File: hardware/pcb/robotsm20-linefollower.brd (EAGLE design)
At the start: 230 x 100 mm, 141 parts, among them Q5 BSS138LT3G, Q6 BSS138LT3G, Q7 BSS138LT3G, Q8 BSS138LT3G, U1 STM32F405RG

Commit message: Change resistor and pinheader to dipswitch for RXTXBT and BOOT12
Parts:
- removed BOOT_SELECT: (no value), CASE-Pinhead:2X03
- removed R19, R20: (no value), rcl:R0603
- added SW1: CTS_219-4LPST, CASE-Switches:DIPSWITCH_4P_SMD
- R17, R18: value (none) -> 10k
- moved R18 218.9 mm to (-91.4, -41.3)
- moved R17 218.8 mm to (-91.4, -36.2), turned to 0 degrees
- moved DEBUG_CONNECTOR 207.3 mm to (23.5, 3.17), turned to 180 degrees
- turned R21 to 0 degrees
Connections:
- net +3V3: now also SW1.A3, SW1.A4; no longer BOOT_SELECT.1, BOOT_SELECT.2
- net DGND: now also R17.1, R18.1; no longer BOOT_SELECT.5, BOOT_SELECT.6
- net N$26: now also R17.2, SW1.B4; no longer BOOT_SELECT.4
- net N$34: now also R18.2, SW1.B3; no longer BOOT_SELECT.3
- net RX: now also SW1.B1; no longer R17.2, R18.2
- net RX_BT: now also SW1.A1; no longer R17.1
- net RX_HEADER: no longer R18.1
- net TX: now also SW1.B2; no longer R19.2, R20.2
- net TX_BT: now also SW1.A2; no longer R19.1
- net TX_HEADER: no longer R20.1
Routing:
- net SWDIO: track 0.00 -> 202.4 mm, vias 0 -> 2
- net SWCLK: track 0.00 -> 202.3 mm, vias 0 -> 2
- net N$1: track 112.5 -> 158.7 mm, vias 0 -> 2
- net SDIO_CMD: track 0.00 -> 13.0 mm
- net SDIO_CK: track 0.00 -> 11.7 mm
- net RX_HEADER: track 16.7 -> 5.18 mm
- net DGND: track 205.4 -> 216.5 mm
- net SDIO_D0: track 0.00 -> 10.8 mm
- net RX: track 48.2 -> 43.0 mm
- net TX: track 49.5 -> 45.9 mm
- net +3V3: track 89.1 -> 86.5 mm
- net BTN_SEL: track 0.00 -> 1.91 mm
- net TX_HEADER: track 19.6 -> 18.1 mm

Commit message: Routed new dipswitch
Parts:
- moved SW1 215.5 mm to (87.0, 79.4), turned to 270 degrees
- moved R41 14.1 mm to (77.5, 86.4), turned to 195 degrees
- moved R42 13.7 mm to (85.7, 88.3), turned to 195 degrees
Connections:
- removed net RX_HEADER: UART_CONNECTOR.1
- removed net TX_HEADER: UART_CONNECTOR.2
- net RX: now also UART_CONNECTOR.1
- net TX: now also UART_CONNECTOR.2
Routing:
- net TX: track 45.9 -> 71.4 mm
- net RX: track 43.0 -> 67.4 mm
- net TX_HEADER: track 18.1 -> 0.00 mm
- net +3V3: track 86.5 -> 71.0 mm
- net TX_BT: track 2.93 -> 8.21 mm, vias 0 -> 1
- net RX_HEADER: track 5.18 -> 0.00 mm
- net RX_BT: track 2.93 -> 7.82 mm

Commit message: Switched RL encoder pins
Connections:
- net ENC_L_A: now also U1.21; no longer U1.15
- net ENC_L_B: now also U1.55; no longer U1.14
- net ENC_R_A: now also U1.15; no longer U1.21
- net ENC_R_B: now also U1.14; no longer U1.55
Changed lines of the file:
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@@
 <contactref element="MOTORDRIVER" pad="41"/>
 <contactref element="U1" pad="59"/>
-<wire x1="141.181" y1="64.346" x2="141.181" y2="66.7137" width="0.254" layer="1"/>
-<wire x1="117.7130625" y1="63.0428" x2="139.8778" y2="63.0428" width="0.254" layer="1"/>
-<wire x1="139.8778" y1="63.0428" x2="141.181" y2="64.346" width="0.254" layer="1"/>
+<wire x1="141.181" y1="64.981" x2="141.181" y2="66.7137" width="0.254" layer="1"/>
+<wire x1="117.7130625" y1="63.0428" x2="139.2428" y2="63.0428" width="0.254" layer="1"/>
+<wire x1="139.2428" y1="63.0428" x2="141.181" y2="64.981" width="0.254" layer="1"/>
 <wire x1="115.802" y1="60.3276" x2="115.802" y2="61.1317375" width="0.254" layer="1"/>
 <wire x1="115.802" y1="61.1317375" x2="117.7130625" y2="63.0428" width="0.254" layer="1"/>
@@
 <contactref element="MOTORDRIVER" pad="42"/>
 <contactref element="U1" pad="58"/>
-<wire x1="140.681" y1="66.7137" x2="140.681" y2="64.481" width="0.254" layer="1"/>
-<wire x1="139.6492" y1="63.4492" x2="117.544725" y2="63.4492" width="0.254" layer="1"/>
+<wire x1="140.681" y1="66.7137" x2="140.681" y2="65.116" width="0.254" layer="1"/>
+<wire x1="139.0142" y1="63.4492" x2="117.544725" y2="63.4492" width="0.254" layer="1"/>
 <wire x1="115.302" y1="61.206475" x2="115.302" y2="60.3276" width="0.254" layer="1"/>
-<wire x1="140.681" y1="64.481" x2="139.6492" y2="63.4492" width="0.254" layer="1"/>
+<wire x1="140.681" y1="65.116" x2="139.0142" y2="63.4492" width="0.254" layer="1"/>
 <wire x1="117.544725" y1="63.4492" x2="115.302" y2="61.206475" width="0.254" layer="1"/>
 </signal>
@@
 <wire x1="107.1" y1="67.31" x2="116.84" y2="85.51" width="0" layer="19" extent="1-1"/>
 <wire x1="86.546034375" y1="88.48499375" x2="91.395" y2="78.105" width="0" layer="19" extent="1-1"/>
-<wire x1="78.291034375" y1="86.57999375" x2="89.0524" y2="67.945" width="0" layer="19" extent="1-1"/>
-<wire x1="59.54220625" y1="77.1517125" x2="78.291034375" y2="86.57999375" width="0" layer="19" extent="1-1"/>
+<wire x1="78.291034375" y1="86.57999375" x2="86.546034375" y2="88.48499375" width="0" layer="19" extent="1-1"/>
+<wire x1="67.89555625" y1="87.04444375" x2="78.291034375" y2="86.57999375" width="0" layer="19" extent="1-1"/>
+<wire x1="59.54220625" y1="77.1517125" x2="67.89555625" y2="87.04444375" width="0" layer="19" extent="1-1"/>
 <wire x1="57.624271875" y1="77.000825" x2="59.54220625" y2="77.1517125" width="0" layer="19" extent="1-1"/>
 <wire x1="51.557565625" y1="80.015775" x2="57.624271875" y2="77.000825" width="0" layer="19" extent="1-1"/>
-<wire x1="67.89555625" y1="87.04444375" x2="59.54220625" y2="77.1517125" width="0" layer="19" extent="1-1"/>
 <wire x1="76.48" y1="129.755" x2="86.546034375" y2="88.48499375" width="0" layer="19" extent="1-1"/>
 <wire x1="-88.265" y1="-22.225" x2="51.557565625" y2="80.015775" width="0" layer="19" extent="1-1"/>
@@
 </signal>
 <signal name="ENC_L_B">
-<contactref element="U1" pad="14"/>
 <contactref element="ENC_L" pad="5"/>
-<wire x1="66.675" y1="29.5" x2="145.6023" y2="75.135" width="0" layer="19" extent="1-1"/>
+<contactref element="U1" pad="55"/>
+<wire x1="66.675" y1="29.5" x2="139.181" y2="66.7137" width="0" layer="19" extent="1-1"/>
 </signal>
 <signal name="VOLTM_BOOST">
@@
 </signal>
 <signal name="ENC_L_A">
-<contactref element="U1" pad="15"/>
 <contactref element="ENC_L" pad="6"/>
-<wire x1="66.675" y1="28" x2="145.6023" y2="75.635" width="0" layer="19" extent="1-1"/>
+<contactref element="U1" pad="21"/>
+<wire x1="66.675" y1="28" x2="141.681" y2="78.0563" width="0" layer="19" extent="1-1"/>
 </signal>
 <signal name="VOLTM_BATT">
@@
 </signal>
 <signal name="ENC_R_A">
-<contactref element="U1" pad="21"/>
 <contactref element="ENC_R" pad="6"/>
-<wire x1="162.56" y1="35.5" x2="141.681" y2="78.0563" width="0" layer="19" extent="1-1"/>
+<contactref element="U1" pad="15"/>
+<wire x1="162.56" y1="35.5" x2="145.6023" y2="75.635" width="0" layer="19" extent="1-1"/>
 </signal>
 <signal name="MUX2">
@@
 </signal>
 <signal name="ENC_R_B">
-<contactref element="U1" pad="55"/>
 <contactref element="ENC_R" pad="5"/>
-<wire x1="162.56" y1="34" x2="139.181" y2="66.7137" width="0" layer="19" extent="1-1"/>
+<contactref element="U1" pad="14"/>
+<wire x1="162.56" y1="34" x2="145.6023" y2="75.135" width="0" layer="19" extent="1-1"/>
 </signal>
 <signal name="SDIO_CK">
@@
 <wire x1="75.1586" y1="80.4164" x2="76.835" y2="80.4164" width="0.254" layer="1"/>
 <wire x1="69.0098375" y1="86.5651625" x2="75.1586" y2="80.4164" width="0.254" layer="1"/>
-<wire x1="76.835" y1="80.4164" x2="138.181" y2="66.7137" width="0" layer="19" extent="1-1"/>
+<wire x1="138.181" y1="66.7137" x2="76.835" y2="80.4164" width="0" layer="19" extent="1-1"/>
 </signal>
 <signal name="BTN_SEL">
@@
 <contactref element="R17" pad="2"/>
 <contactref element="SW1" pad="B4"/>
-<wire x1="-90.59" y1="-36.195" x2="82.595" y2="75.565" width="0" layer="19" extent="1-1"/>
-<wire x1="-77.255" y1="2.54" x2="-90.59" y2="-36.195" width="0" layer="19" extent="1-1"/>
+<wire x1="-77.255" y1="2.54" x2="82.595" y2="75.565" width="0" layer="19" extent="1-1"/>
+<wire x1="-90.59" y1="-36.195" x2="-77.255" y2="2.54" width="0" layer="19" extent="1-1"/>
 </signal>
 <signal name="N$34">
@@
 <contactref element="R18" pad="2"/>
 <contactref element="SW1" pad="B3"/>
-<wire x1="-90.59" y1="-41.275" x2="82.595" y2="78.105" width="0" layer="19" extent="1-1"/>
-<wire x1="-78.955" y1="7.62" x2="-90.59" y2="-41.275" width="0" layer="19" extent="1-1"/>
+<wire x1="-78.955" y1="7.62" x2="82.595" y2="78.105" width="0" layer="19" extent="1-1"/>
+<wire x1="-90.59" y1="-41.275" x2="-78.955" y2="7.62" width="0" layer="19" extent="1-1"/>
 </signal>
 <signal name="MOTOR_R-">
@@
 <wire x1="74.93" y1="80.01" x2="76.835" y2="80.01" width="0.254" layer="1"/>
 <wire x1="69.215" y1="85.725" x2="74.93" y2="80.01" width="0.254" layer="1"/>
-<wire x1="76.835" y1="80.01" x2="138.681" y2="66.7137" width="0" layer="19" extent="1-1"/>
+<wire x1="138.681" y1="66.7137" x2="76.835" y2="80.01" width="0" layer="19" extent="1-1"/>
 </signal>
 <signal name="N$20">
@@
 <wire x1="143.181" y1="66.7137" x2="150.075" y2="69.215" width="0" layer="19" extent="1-1"/>
 <wire x1="143.51" y1="62.015" x2="143.181" y2="66.7137" width="0" layer="19" extent="1-1"/>
-<wire x1="143.181" y1="78.0563" x2="150.075" y2="69.215" width="0" layer="19" extent="1-1"/>
-<wire x1="142.875" y1="82.13" x2="143.181" y2="78.0563" width="0" layer="19" extent="1-1"/>
-<wire x1="137.795" y1="82.13" x2="142.875" y2="82.13" width="0" layer="19" extent="1-1"/>
-<wire x1="135.89" y1="82.13" x2="137.795" y2="82.13" width="0" layer="19" extent="1-1"/>
 <wire x1="129.325" y1="66.675" x2="143.181" y2="66.7137" width="0" layer="19" extent="1-1"/>
-<wire x1="129.325" y1="68.58" x2="129.325" y2="66.675" width="0" layer="19" extent="1-1"/>
-<wire x1="107.1" y1="71.12" x2="129.325" y2="68.58" width="0" layer="19" extent="1-1"/>
-<wire x1="97.86" y1="82.453" x2="107.1" y2="71.12" width="0" layer="19" extent="1-1"/>
-<wire x1="91.225" y1="72.39" x2="97.86" y2="82.453" width="0" layer="19" extent="1-1"/>
-<wire x1="89.0524" y1="70.245" x2="91.225" y2="72.39" width="0" layer="19" extent="1-1"/>
-<wire x1="84.455" y1="67.945" x2="89.0524" y2="70.245" width="0" layer="19" extent="1-1"/>
-<wire x1="84.78" y1="66.895" x2="84.455" y2="67.945" width="0" layer="19" extent="1-1"/>
-<wire x1="85.725" y1="63.285" x2="84.78" y2="66.895" width="0" layer="19" extent="1-1"/>
-<wire x1="83.82" y1="71.97" x2="84.455" y2="67.945" width="0" layer="19" extent="1-1"/>
-<wire x1="81.915" y1="72.705" x2="83.82" y2="71.97" width="0" layer="19" extent="1-1"/>
-<wire x1="92.925" y1="63.5" x2="85.725" y2="63.285" width="0" layer="19" extent="1-1"/>
-<wire x1="111.213" y1="92.253" x2="97.86" y2="82.453" width="0" layer="19" extent="1-1"/>
-<wire x1="68.58" y1="62.23" x2="84.78" y2="66.895" width="0" layer="19" extent="1-1"/>
-<wire x1="56.2476875" y1="76.008084375" x2="68.58" y2="62.23" width="0" layer="19" extent="1-1"/>
-<wire x1="52.36545625" y1="77.172496875" x2="56.2476875" y2="76.008084375" width="0" layer="19" extent="1-1"/>
-<wire x1="70.020590625" y1="88.33295" x2="56.2476875" y2="76.008084375" width="0" layer="19" extent="1-1"/>
-<wire x1="76.960184375" y1="92.06295" x2="70.020590625" y2="88.33295" width="0" layer="19" extent="1-1"/>
 <wire x1="75.78" y1="116.205" x2="76.960184375" y2="92.06295" width="0" layer="19" extent="1-1"/>
 <wire x1="75.88" y1="118.915" x2="75.78" y2="116.205" width="0" layer="19" extent="1-1"/>

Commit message: Routed more compoents
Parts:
- moved U$6 327.9 mm to (222.2, 61.0)
- moved U$4 326.3 mm to (221.6, 61.0), flipped to the bottom
- moved R44 264.3 mm to (162.6, 76.8)
- moved R43 263.4 mm to (162.6, 78.7), turned to 180 degrees
- moved R18 210.4 mm to (80.0, 80.6)
- moved R17 205.4 mm to (80.0, 76.8)
- moved C40 203.2 mm to (149.2, 62.9), turned to 270 degrees
- moved C13 194.1 mm to (108.5, 8.64), turned to 180 degrees
- moved R16 173.9 mm to (80.0, 74.9)
- moved R13 173.4 mm to (80.0, 78.7), turned to 180 degrees
- moved LED1 117.1 mm to (147.3, 36.8), turned to 180 degrees
- moved R38 112.7 mm to (149.9, 41.9), turned to 270 degrees
- moved R36 109.3 mm to (147.3, 41.9), turned to 270 degrees
- moved Q6 109.2 mm to (151.1, 45.7), turned to 180 degrees
- moved R40 106.0 mm to (144.8, 41.9), turned to 270 degrees
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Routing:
- net V+: track 231.0 -> 362.8 mm
- net ENC_L_A: track 0.00 -> 113.3 mm, vias 0 -> 9
- net ENC_L_B: track 0.00 -> 109.8 mm, vias 0 -> 7
- net PWM_FAN_L: track 0.00 -> 95.3 mm, vias 0 -> 4
- net SDIO_CMD: track 13.0 -> 101.1 mm, vias 0 -> 4
- net SDIO_CK: track 11.7 -> 95.2 mm, vias 0 -> 4
- net BUZZER: track 6.18 -> 85.1 mm, vias 0 -> 2
- net SDIO_D0: track 10.8 -> 81.6 mm, vias 0 -> 2
- net BOOT0: track 0.00 -> 70.6 mm, vias 0 -> 2
- net DGND: track 216.5 -> 285.3 mm, vias 0 -> 5
- net BOOT1: track 0.00 -> 63.3 mm, vias 0 -> 2
- net ENC_R_B: track 0.00 -> 54.8 mm, vias 0 -> 2
- net ENC_R_A: track 0.00 -> 53.7 mm, vias 0 -> 2
- net !RESET: track 83.5 -> 137.1 mm, vias 0 -> 3
- net PWM_FAN_R: track 0.00 -> 43.7 mm, vias 0 -> 2
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
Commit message: Changed testpoint to TH and rerouted due to change in design
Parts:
- TP_12V, TP_1V8, TP_3V3, TP_5V: value TEST-POINT3X5 -> TEST_POINTPAD_HOLE; device Isaks Bibliotek:PAD.03X.05 -> MISC:PAD_HOLE
- moved TP_3V3 54.6 mm to (-31.1, -9.53)
- moved TP_5V 54.6 mm to (-31.1, -5.71)
- moved TP_12V 48.9 mm to (-31.1, -11.4)
- moved TP_1V8 48.9 mm to (-31.1, -7.62)
- moved LED2 15.3 mm to (204.5, 5.71)
- moved BTN_RESET 2.35 mm to (217.5, 11.0), turned to 90 degrees
- moved BTN_SEL 1.54 mm to (12.3, 12.3), turned to 270 degrees
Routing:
- net SWCLK: track 202.3 -> 157.8 mm
- net SWDIO: track 203.7 -> 162.2 mm
- net DGND: track 285.3 -> 266.4 mm
- net N$38: track 25.9 -> 10.4 mm
- net N$1: track 158.7 -> 146.6 mm
- net !RESET: track 137.1 -> 126.8 mm
- net V+: track 362.8 -> 371.2 mm
- net N$41: track 42.5 -> 39.8 mm
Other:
- outline, holes or cut-outs redrawn

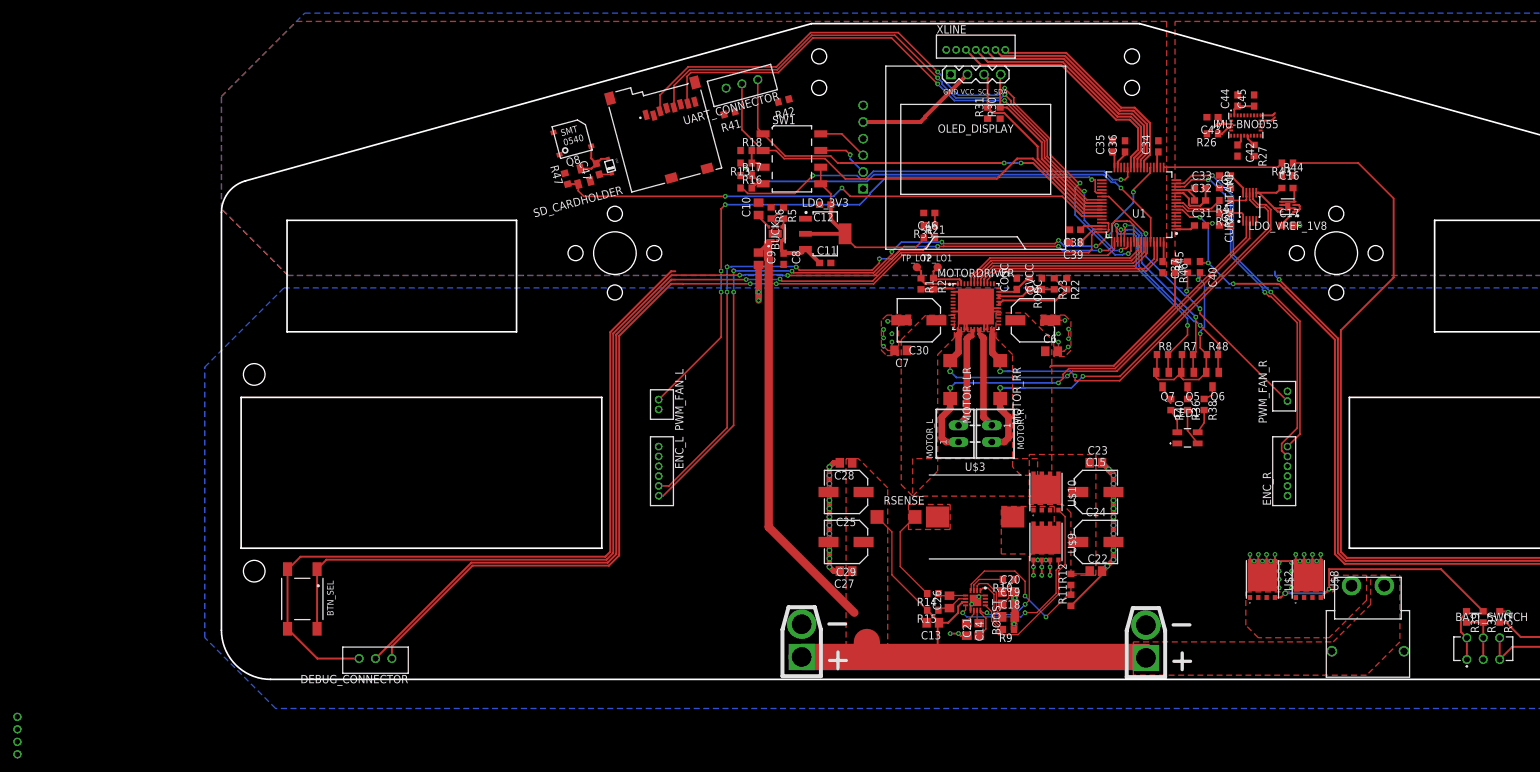
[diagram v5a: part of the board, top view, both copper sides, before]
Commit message: Connection more airwires <3
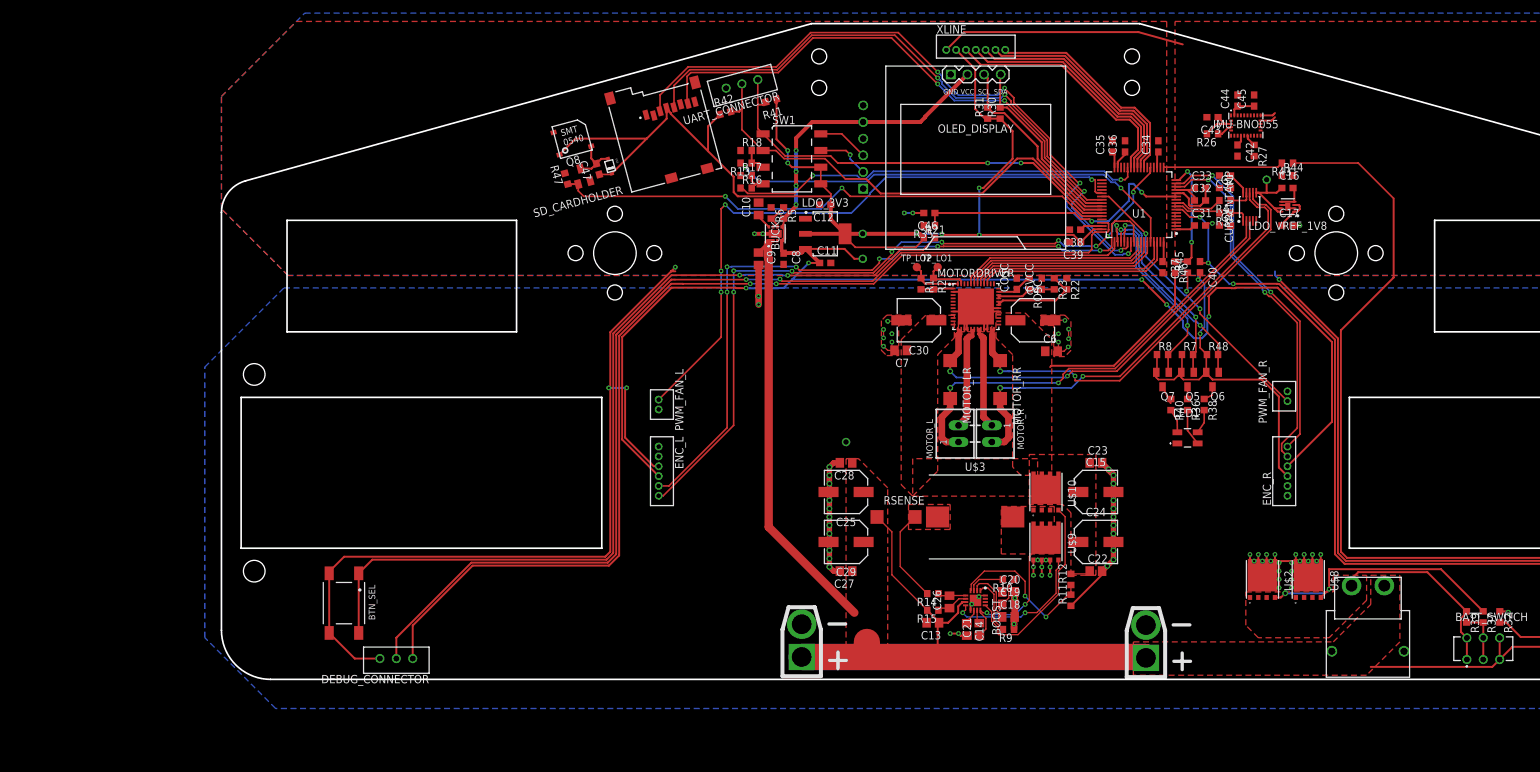
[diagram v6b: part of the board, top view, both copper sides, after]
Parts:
- moved TP_1V8 208.1 mm to (159.4, 76.2)
- moved TP_3V3 150.4 mm to (97.8, 67.9)
- moved TP_5V 146.6 mm to (97.8, 64.1)
- moved TP_12V 135.0 mm to (95.2, 36.2)
- moved R42 9.09 mm to (76.8, 86.4), turned to 15 degrees
- moved R41 6.63 mm to (83.8, 88.3)
- moved BTN_SEL 6.38 mm to (18.7, 11.6)
- moved DEBUG_CONNECTOR 3.18 mm to (26.7, 3.17)
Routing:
- net +5V: track 31.7 -> 242.0 mm, vias 0 -> 9
- net +3V3: track 73.3 -> 231.8 mm, vias 0 -> 6
- net BTN_SEL: track 1.91 -> 43.9 mm, vias 0 -> 2
- net DGND: track 266.4 -> 307.0 mm, vias 5 -> 12
- net AGND: track 17.0 -> 54.5 mm
- net BAT-: track 8.08 -> 29.5 mm
- net V+: track 371.2 -> 391.3 mm
- net VOLTM_BOOST: track 1.91 -> 18.4 mm, vias 0 -> 2
- net N$1: track 146.6 -> 140.5 mm
- net TX: track 69.5 -> 73.2 mm
- net VREF: track 10.2 -> 12.2 mm
- net SDIO_CK: track 95.2 -> 96.8 mm
- net BUZZER: track 85.1 -> 86.7 mm
- net RX: track 65.5 -> 66.9 mm
- net SWDIO: track 162.2 -> 160.8 mm
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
